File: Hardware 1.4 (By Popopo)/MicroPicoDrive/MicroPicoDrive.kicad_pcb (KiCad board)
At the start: 2 copper layers, 63.1 x 55.9 mm, 24 parts, among them IC1 SN74LVC1T45DBVR, IC2 SN74LVC1T45DBVR, IC3 TXU0304QPWRQ1, J1 Conn_02x16, J2 QL_CONN, Q1 Q_NPN_BEC, U1 LM7805_TO220, U2 Pico

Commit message: adding diode VSYS
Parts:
- added D1: B240, Diode_SMD:D_SMB, F.Cu at (129.1, 101.2)
- added REF**: C_1206_3216Metric, Capacitor_SMD:C_1206_3216Metric, F.Cu at (106.1, 95.8)
- moved C1 0.14 mm to (149.4, 101.6)
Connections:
- U2 pad 39: +5V -> Net-(D1-K)
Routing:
- net +5V: track 81.6 -> 70.6 mm, vias 6 -> 4
- net Net-(D1-K): track 0.00 -> 8.13 mm
- net +3V3: track 72.6 -> 76.0 mm, vias 2 -> 3
- net GND: vias 27 -> 34
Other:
- board text added: "2024 Ver. 1.4.f"
- board text removed: "2024 Ver. 1.4.e"

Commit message: new rev.f ready
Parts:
- removed the REF** at (106.1, 95.8)
- added ?: , , F.Cu at (123.0, 76.6)
- added ?: , , F.Cu at (178.1, 76.6)
- added ?: , , F.Cu at (178.1, 129.2)
- added ?: , , F.Cu at (120.5, 129.2)
- added G***: LOGO, MDP_Footprints:QR_Code_MDP, B.Cu at (165.9, 124.0)
- moved REF** 12.9 mm to (174.9, 114.0), turned to -90 degrees
- moved REF** 1.37 mm to (174.8, 125.0)
- moved Q1 0.12 mm to (129.1, 114.4)
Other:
- board text added: "2026 Ver. 1.4.f"
- board text removed: "2024 Ver. 1.4.f"

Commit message: recovering hard format
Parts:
- added R4: 330R, Resistor_SMD:R_0603_1608Metric, B.Cu at (170.0, 86.9)
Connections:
- J1 pad 16: unconnected-(J1-Pin_16-Pad16) -> GND
- U2 pad 20: /UI_DETECT -> Net-(U2-GPIO15)
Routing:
- net Net-(U2-GPIO15): track 0.00 -> 3.92 mm
- net /UI_SD_MISO: track 21.3 -> 25.0 mm

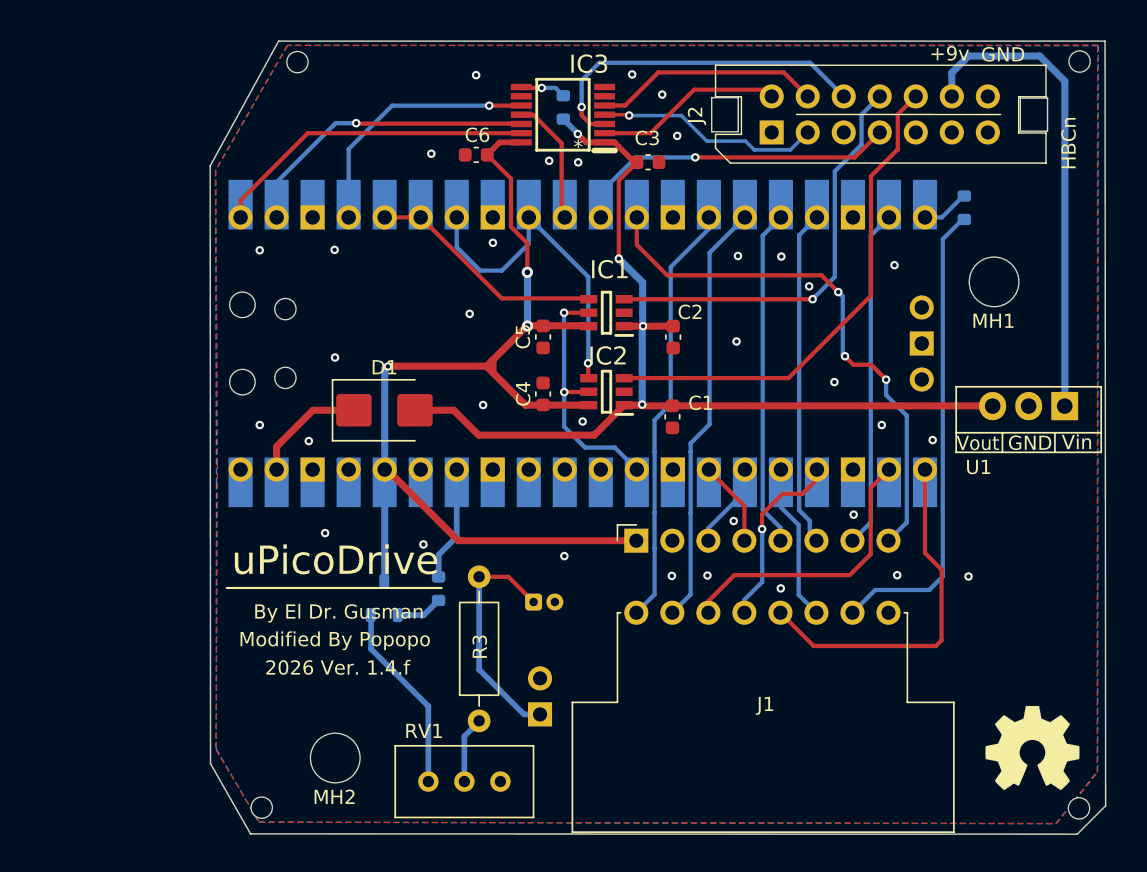
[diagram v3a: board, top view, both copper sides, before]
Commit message: changing DRC and PCB references 1
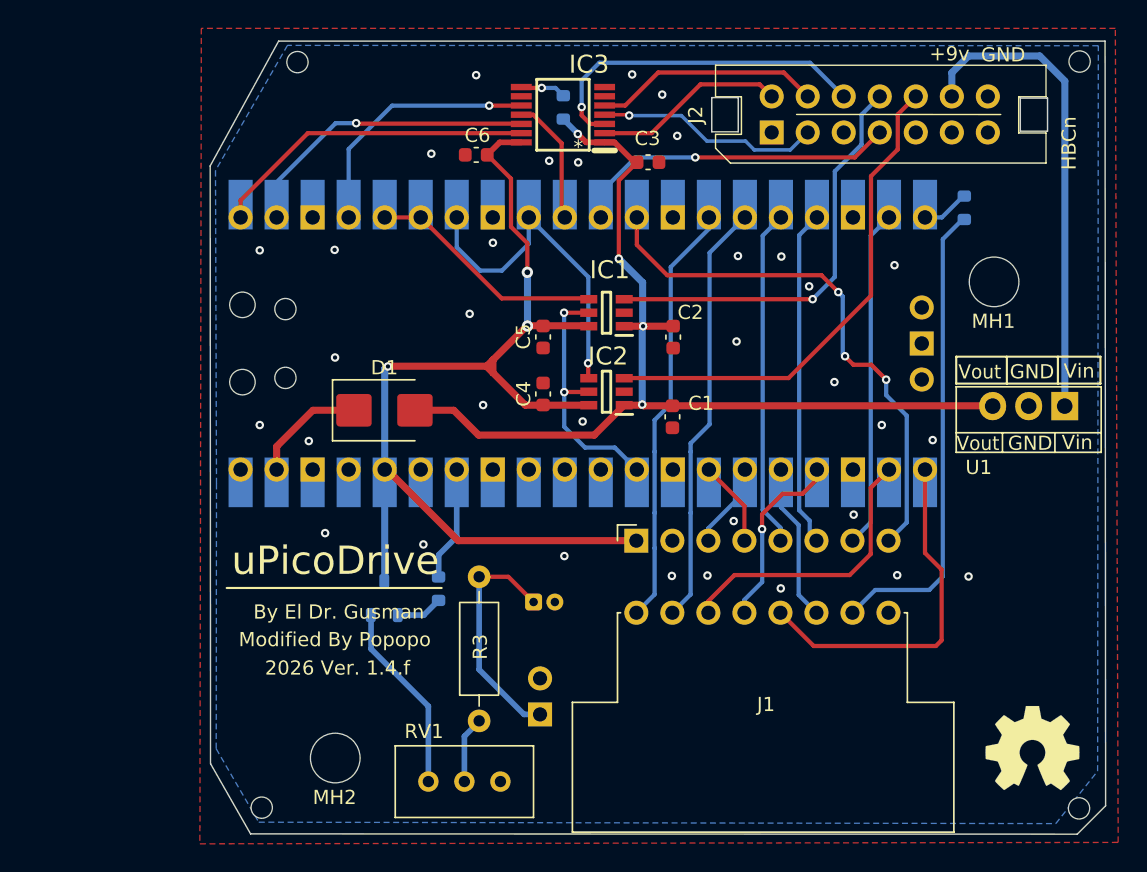
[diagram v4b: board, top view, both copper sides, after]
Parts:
- renumbered REF** to Log_KiCad, REF** to Log_OpenHardware
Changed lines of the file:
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@@
 		(descr "Open Source Hardware Symbol")
 		(tags "Logo Symbol OSHW")
-		(property "Reference" "REF**"
+		(property "Reference" "Log_OpenHardware"
 			(at 0 0 0)
 			(layer "F.SilkS")
@@
 			)
 		)
-		(attr exclude_from_pos_files exclude_from_bom allow_missing_courtyard)
+		(attr board_only exclude_from_pos_files exclude_from_bom allow_missing_courtyard)
 		(fp_poly
 			(pts
@@
 		(descr "KiCad Logo")
 		(tags "Logo KiCad")
-		(property "Reference" "REF**"
+		(property "Reference" "Log_KiCad"
 			(at 0 5.08 90)
 			(layer "B.SilkS")
@@
 			)
 		)
-		(attr exclude_from_pos_files exclude_from_bom allow_missing_courtyard)
+		(attr board_only exclude_from_pos_files exclude_from_bom allow_missing_courtyard)
 		(fp_poly
 			(pts
@@
 	)
 	(gr_line
+		(start 169.43 97.4)
+		(end 169.43 99.3)
+		(stroke
+			(width 0.15)
+			(type solid)
+		)
+		(layer "F.SilkS")
+	)
+	(gr_line
+		(start 169.43 97.4)
+		(end 179.6 97.4)
+		(stroke
+			(width 0.15)
+			(type default)
+		)
+		(layer "F.SilkS")
+	)
+	(gr_line
+		(start 169.43 99.3)
+		(end 179.6 99.3)
+		(stroke
+			(width 0.15)
+			(type default)
+		)
+		(layer "F.SilkS")
+	)
+	(gr_line
+		(start 173 97.4)
+		(end 173 99.3)
+		(stroke
+			(width 0.15)
+			(type solid)
+		)
+		(layer "F.SilkS")
+	)
+	(gr_line
+		(start 176.6 97.4)
+		(end 176.6 99.3)
+		(stroke
+			(width 0.15)
+			(type solid)
+		)
+		(layer "F.SilkS")
+	)
+	(gr_line
+		(start 179.6 97.4)
+		(end 179.6 99.3)
+		(stroke
+			(width 0.15)
+			(type solid)
+		)
+		(layer "F.SilkS")
+	)
+	(gr_line
 		(start 116.825 83.95)
 		(end 116.85 126.1)
@@
 		)
 	)
+	(gr_text "Vout"
+		(at 169.58 99.06 0)
+		(layer "F.SilkS")
+		(effects
+			(font
+				(size 1 0.95)
+				(thickness 0.15)
+			)
+			(justify left bottom)
+		)
+	)
 	(gr_text "*"
 		(at 142.44 83.21 0)
@@
 		)
 	)
+	(gr_text "GND"
+		(at 173.2 99.05 0)
+		(layer "F.SilkS")
+		(effects
+			(font
+				(size 1 1)
+				(thickness 0.15)
+			)
+			(justify left bottom)
+		)
+	)
 	(gr_text "Vin"
 		(at 176.87 104.04 0)
@@
 		)
 	)
+	(gr_text "Vin"
+		(at 177 99 0)
+		(layer "F.SilkS")
+		(effects
+			(font
+				(size 1 1)
+				(thickness 0.15)
+			)
+			(justify left bottom)
+		)
+	)
 	(gr_text "Modified By Popopo"
 		(at 125.61 117.35 0)
@@
 	)
 	(segment
-		(start 147.880421 81.639579)
+		(start 147.960421 81.639579)
 		(end 144.638 81.639579)
 		(width 0.3)
@@
 	)
 	(segment
-		(start 156.42 79.05)
-		(end 155.945 78.575)
+		(start 151.4 78.2)
+		(end 147.960421 81.639579)
 		(width 0.3)
 		(layer "F.Cu")
@@
 	)
 	(segment
-		(start 155.945 78.575)
-		(end 150.945 78.575)
+		(start 156.42 79.05)
+		(end 155.57 78.2)
 		(width 0.3)
 		(layer "F.Cu")
@@
 	)
 	(segment
-		(start 150.945 78.575)
-		(end 147.880421 81.639579)
+		(start 155.57 78.2)
+		(end 151.4 78.2)
 		(width 0.3)
 		(layer "F.Cu")
@@
 		(polygon
 			(pts
-				(xy 117.225 84.225) (xy 117.3375 104.925) (xy 117.25 125.15) (xy 120.3 130.225) (xy 176.495 130.325)
-				(xy 179.37 126.75) (xy 179.4 75.425) (xy 122.275 75.45)
+				(xy 116.1 131.75) (xy 180.85 131.65) (xy 180.65 74.25) (xy 116.2 74.25)
 			)
 		)
@@
 		)
 	)
+	(group ""
+		(members "9abdc5de-a996-407d-a428-281bdf8a19ea" "c80fd9e5-bf70-4d36-bf48-18e4ee7066aa"
+			"d5606334-7175-4ede-854b-10cd1030aaed"
+		)
+	)

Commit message: changing DRC and PCB references 2
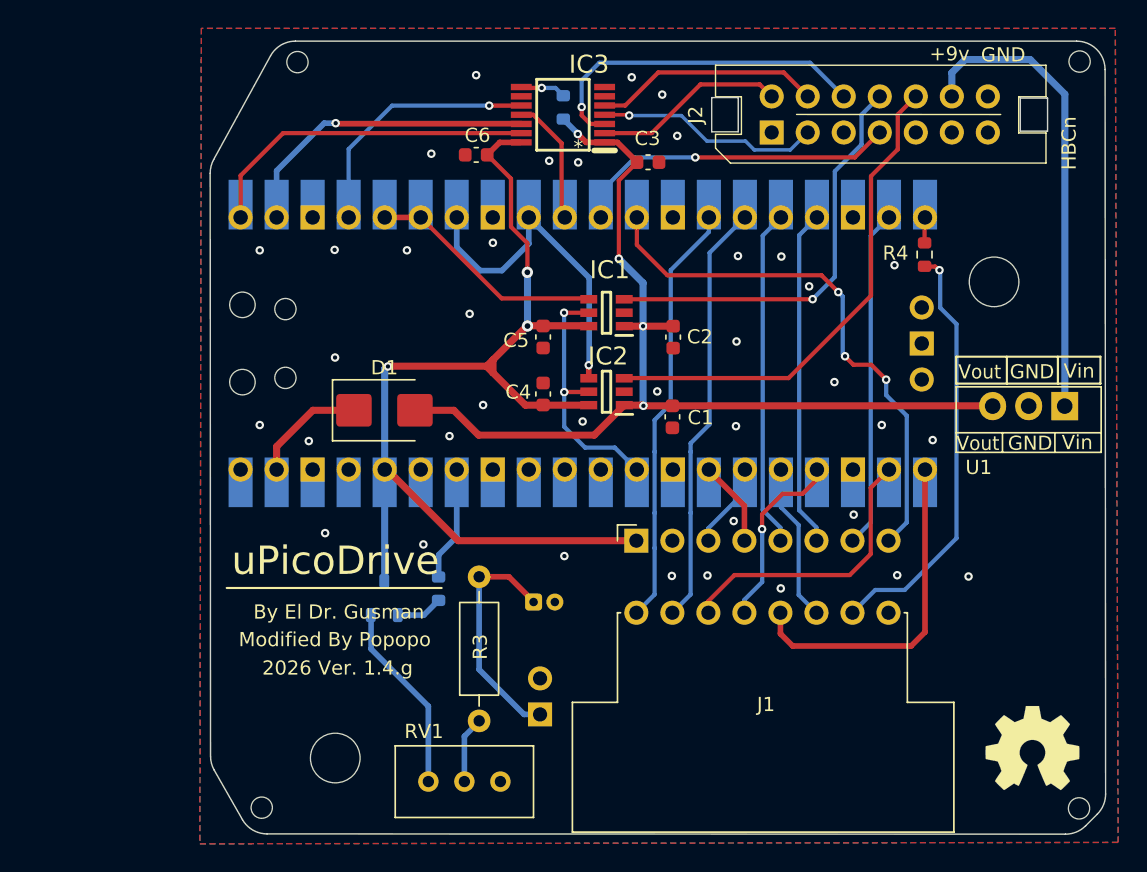
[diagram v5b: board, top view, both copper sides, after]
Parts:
- MH_S1, MH_S2, MH_S3, MH_S4: renamed from ?; value (none) -> MountingHole
- R4: value 330R -> 1K; moved to F.Cu
- moved R4 4.33 mm to (167.2, 90.2)
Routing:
- net /UI_DETECT: track 33.3 -> 30.1 mm, vias 0 -> 1
- net Net-(U2-GPIO15): track 3.92 -> 2.33 mm
- net /UI_SD_MISO: track 25.0 -> 23.9 mm
- net /PICO_CS_IN: track 23.0 -> 24.0 mm
- net +9V: track 33.8 -> 33.0 mm
- net GND: vias 34 -> 38
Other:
- outline, holes or cut-outs redrawn
- board text added: "2026 Ver. 1.4.g"
- board text removed: "2026 Ver. 1.4.f"
